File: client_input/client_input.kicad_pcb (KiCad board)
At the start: 2 copper layers, 10 parts, among them P1 CONN_01X06, P2 CONN_01X08, SW1 DIPS_08, SW2 SW_PUSH, SW3 SW_PUSH, U1 ESP-12_Breakout, U2 MCP23017, U3 MCP3208, U4 WS2812B

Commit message: PCD laid out.
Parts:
- removed U4: WS2812B, LEDs:LED_RGB_PLLC-6
- added D1: WS2812B, LEDs:LED_RGB_PLLC-6, F.Cu at (148.6, 71.1)
- added D2: Green, LEDs:LED-3MM, F.Cu at (254.6, 130.2)
- added D3: Yellow, LEDs:LED-3MM, F.Cu at (254.6, 122.6)
- added D4: Status RGB, LEDs:LED-RGB-5MM_Common_Cathode, F.Cu at (273.1, 148.6)
- added D5: Red, LEDs:LED-3MM, F.Cu at (254.6, 114.9)
- added P3: Ribbon, Socket_Strips:Socket_Strip_Straight_1x09, F.Cu at (185.4, 80.0)
- added P4: Ribbon, Socket_Strips:Socket_Strip_Straight_1x08, F.Cu at (167.6, 82.5)
- added P6: Ribbon, Socket_Strips:Socket_Strip_Straight_1x04, F.Cu at (243.8, 148.6)
- added P7: Ribbon, Socket_Strips:Socket_Strip_Straight_1x09, F.Cu at (243.8, 83.8)
- added P8: Ribbon, Socket_Strips:Socket_Strip_Straight_1x03, F.Cu at (244.5, 120.0)
- added R2: 22k, Resistors_ThroughHole:Resistor_Horizontal_RM10mm, F.Cu at (143.5, 109.2)
- added R3: 560, Resistors_ThroughHole:Resistor_Horizontal_RM10mm, F.Cu at (158.8, 109.2)
- added R4: 470, Resistors_ThroughHole:Resistor_Horizontal_RM10mm, F.Cu at (262.9, 151.1)
- added R5: 100, Resistors_ThroughHole:Resistor_Horizontal_RM10mm, F.Cu at (262.9, 141.0)
- added R6: 100, Resistors_ThroughHole:Resistor_Horizontal_RM10mm, F.Cu at (262.9, 146.1)
- added R7: 100, Resistors_ThroughHole:Resistor_Horizontal_RM10mm, F.Cu at (263.5, 130.2)
- added R8: 100, Resistors_ThroughHole:Resistor_Horizontal_RM10mm, F.Cu at (263.5, 122.6)
- added R9: 470, Resistors_ThroughHole:Resistor_Horizontal_RM10mm, F.Cu at (263.5, 114.9)
- added SW4: DIPS_08, Buttons_Switches_ThroughHole:SW_DIP_x8_Slide, F.Cu at (250.2, 83.8)
- P1: value CONN_01X06 -> Analog In; footprint Pin_Headers:Pin_Header_Angled_1x06 -> Socket_Strips:Socket_Strip_Straight_1x08
- P2: value CONN_01X08 -> FTDI; footprint Socket_Strips:Socket_Strip_Straight_1x08 -> Pin_Headers:Pin_Header_Straight_1x06
- R1: value 570 -> 100k
- SW1: value DIPS_08 -> PAIR_MODE; footprint Buttons_Switches_ThroughHole:SW_DIP_x8_Slide -> Buttons_Switches_ThroughHole:SW_TH_Tactile_Omron_B3F-10xx
- SW2: value SW_PUSH -> RESET
- SW3: value SW_PUSH -> Bootload
- U1: value ESP-12_Breakout -> MCP3208; footprint ESP8266:ESP12_Breakout -> Housings_DIP:DIP-16_W7.62mm_LongPads
- U2: value MCP23017 -> ESP-12_Breakout; footprint Housings_DIP:DIP-28_W7.62mm_LongPads -> ESP8266:ESP12_Breakout
- U3: value MCP3208 -> MCP23017; footprint Housings_DIP:DIP-18_W7.62mm_LongPads -> Housings_DIP:DIP-28_W7.62mm_LongPads
- moved U3 87.8 mm to (172.7, 80.0)
- moved SW3 50.7 mm to (147.3, 83.8), turned to 90 degrees
- moved SW2 49.9 mm to (138.4, 77.5), turned to 270 degrees
- moved U2 46.6 mm to (148.5, 105.0), turned to 270 degrees
- moved P2 37.0 mm to (116.8, 78.7), turned to 90 degrees
- moved P1 32.1 mm to (116.8, 95.2), turned to 270 degrees
- moved SW1 23.3 mm to (162.6, 77.5)
- moved R1 19.9 mm to (138.4, 109.2)
- moved U1 13.5 mm to (121.9, 95.2), turned to 0 degrees
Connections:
- P1 pad 1: GND -> Net-(P1-Pad1)
- P1 pad 3: +BATT -> Net-(P1-Pad3)
- P2 pad 1: Net-(P2-Pad1) -> GND
- P2 pad 3: Net-(P2-Pad3) -> +BATT
- R1 pad 1: Net-(R1-Pad1) -> +BATT
- R1 pad 2: Net-(R1-Pad2) -> BattSense
- SW1 pad 1: Net-(SW1-Pad1) -> Pair_sw
- SW1 pad 2: Net-(SW1-Pad2) -> GND
- SW1 pad 3: Net-(SW1-Pad3) -> (no net)
- SW1 pad 4: Net-(SW1-Pad4) -> (no net)
- U1 pad 1: Net-(SW2-Pad2) -> Net-(P1-Pad1)
- U1 pad 11: Net-(R1-Pad1) -> Net-(U1-Pad11)
- U1 pad 12: Net-(SW3-Pad1) -> Net-(U1-Pad12)
- U1 pad 14: Net-(U1-Pad14) -> GND
- U1 pad 15: Net-(P1-Pad4) -> +3V3
- U1 pad 16: Net-(P1-Pad5) -> +3V3
- U1 pad 2: BattSense -> Net-(P1-Pad2)
- U1 pad 3: Net-(U1-Pad3) -> Net-(P1-Pad3)
- U1 pad 4: Net-(U1-Pad4) -> Net-(P1-Pad4)
- U1 pad 5: Net-(U1-Pad5) -> Net-(P1-Pad5)
- U1 pad 6: Net-(U1-Pad6) -> Net-(P1-Pad6)
- U1 pad 7: Net-(U1-Pad7) -> Net-(P1-Pad7)
- U1 pad 8: +BATT -> Net-(P1-Pad8)
- U2 pad 1: Net-(U2-Pad1) -> Net-(SW2-Pad2)
- U2 pad 10: GND -> Net-(U1-Pad10)
- U2 pad 11: (no net) -> Net-(R3-Pad1)
- U2 pad 12: Net-(U1-Pad14) -> Net-(SW3-Pad1)
- U2 pad 13: Net-(U1-Pad13) -> Net-(U2-Pad13)
- U2 pad 14: (no net) -> Net-(U2-Pad14)
- U2 pad 15: GND -> Net-(P2-Pad4)
- U2 pad 16: GND -> Net-(P2-Pad5)
- U2 pad 2: Net-(U2-Pad2) -> BattSense
- U2 pad 4: Net-(U2-Pad4) -> Net-(SW2-Pad2)
- U2 pad 5: Net-(U2-Pad5) -> Net-(U1-Pad13)
- U2 pad 6: Net-(U2-Pad6) -> Net-(U1-Pad12)
- U2 pad 7: Net-(U2-Pad7) -> Net-(U1-Pad11)
- U2 pad 8: Net-(U2-Pad8) -> +BATT
- U2 pad 9: +3V3 -> GND
- U3 pad 1: Net-(P2-Pad1) -> Pair_sw
- U3 pad 10: Net-(U1-Pad10) -> GND
- U3 pad 11: Net-(U1-Pad7) -> (no net)
- U3 pad 12: Net-(U1-Pad6) -> Net-(U2-Pad14)
- U3 pad 13: Net-(U1-Pad5) -> Net-(U2-Pad13)
- U3 pad 14: GND -> (no net)
- U3 pad 15: +3V3 -> GND
- U3 pad 16: +3V3 -> GND
- U3 pad 17: (no net) -> GND
- U3 pad 18: (no net) -> +3V3
- U3 pad 2: Net-(P2-Pad2) -> Net-(P4-Pad1)
- U3 pad 3: Net-(P2-Pad3) -> Net-(P4-Pad2)
- U3 pad 4: Net-(P2-Pad4) -> Net-(P4-Pad3)
- U3 pad 5: Net-(P2-Pad5) -> Net-(P4-Pad4)
- U3 pad 6: Net-(P2-Pad6) -> Net-(P4-Pad5)
- U3 pad 7: Net-(P2-Pad7) -> Net-(P4-Pad6)
- U3 pad 8: Net-(P2-Pad8) -> Net-(P4-Pad7)
- U3 pad 9: GND -> +3V3

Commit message: Made some tweaks, outputted test gerber files (still PTH version).
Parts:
- added P9: LiPo, Socket_Strips:Socket_Strip_Straight_1x02, F.Cu at (129.5, 81.3)
- D1: footprint LEDs:LED_RGB_PLLC-6 -> LEDs:LED_NEOPIXEL
- SW1, SW2, SW3: footprint Buttons_Switches_ThroughHole:SW_TH_Tactile_Omron_B3F-10xx -> Buttons_Switches_ThroughHole:SW_PUSH_SMALL
- moved SW1 44.6 mm to (158.8, 121.9), turned to 180 degrees
- moved SW2 44.5 mm to (138.4, 121.9), turned to 180 degrees
- moved SW3 38.1 mm to (148.6, 121.9), turned to 180 degrees
- moved D1 30.1 mm to (125.6, 90.5), turned to 270 degrees
- moved P2 25.5 mm to (142.2, 81.3)
- moved P4 4.58 mm to (170.2, 86.4)
- moved P3 4.58 mm to (188.0, 83.8)
- moved U3 4.58 mm to (175.3, 83.8)
- moved P1 3.81 mm to (116.8, 99.1)
- moved R3 3.81 mm to (154.9, 109.2)
- moved U1 3.81 mm to (121.9, 99.1)
- moved R2 1.27 mm to (144.8, 109.2)
- moved R1 1.27 mm to (139.7, 109.2)
- moved U2 0.43 mm to (148.6, 105.4)
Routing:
- net GND: track 0.00 -> 157.2 mm
- net Pair_sw: track 0.00 -> 88.9 mm
- net +3V3: track 0.00 -> 78.7 mm
- net Net-(U1-Pad10): track 0.00 -> 61.0 mm
- net Net-(SW2-Pad2): track 0.00 -> 55.7 mm
- net +BATT: track 0.00 -> 38.3 mm
- net Net-(D1-Pad4): track 0.00 -> 36.1 mm
- net Net-(SW3-Pad1): track 0.00 -> 33.0 mm
- net Net-(P2-Pad4): track 0.00 -> 30.5 mm
- net Net-(P2-Pad5): track 0.00 -> 25.4 mm
- net Net-(U2-Pad14): track 0.00 -> 22.9 mm
- net Net-(U2-Pad13): track 0.00 -> 22.9 mm
- net BattSense: track 0.00 -> 10.1 mm
- net Net-(R3-Pad1): track 0.00 -> 7.62 mm
- net Net-(U1-Pad13): track 0.00 -> 5.18 mm
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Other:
- board outline added: 81.3 x 52.1 mm
- net class Default: trace_width 0.25 -> 1

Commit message: version 2.0, lots of changes. (smd parts, 2 sided, production ready)
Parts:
- removed D2: Green, LEDs:LED-3MM
- removed D3: Yellow, LEDs:LED-3MM
- removed D4: Status RGB, LEDs:LED-RGB-5MM_Common_Cathode
- removed D5: Red, LEDs:LED-3MM
- removed P3: Ribbon, Socket_Strips:Socket_Strip_Straight_1x09
- removed R5, R6, R7, R8: 100, Resistors_ThroughHole:Resistor_Horizontal_RM10mm
- removed R9: 470, Resistors_ThroughHole:Resistor_Horizontal_RM10mm
- removed SW4: DIPS_08, Buttons_Switches_ThroughHole:SW_DIP_x8_Slide
- added ?: BATT/FTDI, Buttons_Switches_ThroughHole:SW_Micro_SPST, F.Cu at (13.1, 4.38)
- added C1: 2.2uF, Capacitors_ThroughHole:C_Disc_D3_P2.5, F.Cu at (13.1, 19.6)
- added P5: LiPo, Socket_Strips:Socket_Strip_Straight_1x02, F.Cu at (6.76, 4.38)
- added RR1: 10k, Resistors_ThroughHole:Resistor_Array_SIP5, F.Cu at (23.2, 19.6)
- added SW5: , Buttons_Switches_ThroughHole:SW_Micro_SPST, F.Cu at (13.1, 1.84)
- added U4: MCP1700-3302, TO_SOT_Packages_SMD:SOT89-3_Housing_Handsoldering, B.Cu at (7.25, 18.4)
- added U5: MCP23017, Housings_SOIC:SOIC-28_7.5x17.9mm_Pitch1.27mm, F.Cu at (36.6, 17.7)
- added U6: MCP23017, Housings_SOIC:SOIC-28_7.5x17.9mm_Pitch1.27mm, F.Cu at (36.6, 38.0)
- P1: value Analog In -> Analog In 7-0
- P2: value FTDI -> Analog In 15-8; footprint Pin_Headers:Pin_Header_Straight_1x06 -> Socket_Strips:Socket_Strip_Straight_1x08
- P4: value Ribbon -> FTDI; footprint Socket_Strips:Socket_Strip_Straight_1x08 -> Pin_Headers:Pin_Header_Straight_1x06
- P6: value Ribbon -> i/o 0-7; footprint Socket_Strips:Socket_Strip_Straight_1x04 -> Socket_Strips:Socket_Strip_Straight_1x09
- P7: value Ribbon -> i/o 9-15; footprint Socket_Strips:Socket_Strip_Straight_1x09 -> Socket_Strips:Socket_Strip_Straight_1x08
- P8: value Ribbon -> i/o 15-23; footprint Socket_Strips:Socket_Strip_Straight_1x03 -> Socket_Strips:Socket_Strip_Straight_1x09
- P9: value LiPo -> i/o 24-31; footprint Socket_Strips:Socket_Strip_Straight_1x02 -> Socket_Strips:Socket_Strip_Straight_1x09
- R1: value 100k -> 10k; footprint Resistors_ThroughHole:Resistor_Horizontal_RM10mm -> Discret:R4
- R2: value 22k -> 560; footprint Resistors_ThroughHole:Resistor_Horizontal_RM10mm -> Discret:R4
- R3: value 560 -> 100k; footprint Resistors_ThroughHole:Resistor_Horizontal_RM10mm -> Discret:R4
- R4: value 470 -> 22k; footprint Resistors_ThroughHole:Resistor_Horizontal_RM10mm -> Discret:R4
- SW1: value PAIR_MODE -> RST
- SW2: value RESET -> PAIR
- SW3: value Bootload -> BTLD
- U1: footprint Housings_DIP:DIP-16_W7.62mm_LongPads -> Housings_SOIC:SOIC-16_3.9x9.9mm_Pitch1.27mm
- U2: value ESP-12_Breakout -> MCP3208; footprint ESP8266:ESP12_Breakout -> Housings_SOIC:SOIC-16_3.9x9.9mm_Pitch1.27mm
- U3: value MCP23017 -> ESP-12E; footprint Housings_DIP:DIP-28_W7.62mm_LongPads -> ESP8266:ESP-12E_Brendan; moved to B.Cu
- moved R4 286.9 mm to (10.6, 14.5), turned to 0 degrees
- moved P6 260.8 mm to (23.2, 9.46), turned to 0 degrees
- moved P8 238.9 mm to (23.2, 29.8), turned to 0 degrees
- moved P7 225.6 mm to (25.8, 26.0), turned to 0 degrees
- moved SW1 179.3 mm to (24.0, 3.66), turned to 0 degrees
- moved U3 175.8 mm to (5.21, 39.1)
- moved R3 174.1 mm to (10.6, 12.0), turned to 0 degrees
- moved P4 170.8 mm to (18.2, 8.57)
- moved SW3 165.5 mm to (32.9, 3.66), turned to 0 degrees
- moved U2 158.3 mm to (7.90, 33.0), turned to 0 degrees
- moved SW2 152.7 mm to (41.8, 3.66), turned to 0 degrees
- moved P2 150.3 mm to (1.55, 28.5), turned to 270 degrees
- moved P1 146.8 mm to (1.55, 8.19)
- moved R1 145.7 mm to (25.8, 18.4)
- moved R2 141.2 mm to (23.2, 37.4), turned to 270 degrees
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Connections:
- D1 pad 1: +BATT -> +Vin
- P2 pad 1: GND -> Net-(P2-Pad1)
- P2 pad 3: +BATT -> Net-(P2-Pad3)
- P4 pad 1: Net-(P4-Pad1) -> GND
- P4 pad 3: Net-(P4-Pad3) -> FTDI_VCC
- P6 pad 4: +3V3 -> Net-(P6-Pad4)
- P7 pad 8: Net-(P7-Pad8) -> +3V3
- P9 pad 1: GND -> Net-(P9-Pad1)
- P9 pad 2: +BATT -> Net-(P9-Pad2)
- R1 pad 1: +BATT -> SPI_SS
- R1 pad 2: BattSense -> GND
- R2 pad 1: GND -> LED_stat
- R2 pad 2: BattSense -> Net-(D1-Pad4)
- R3 pad 1: Net-(R3-Pad1) -> +BATT
- R3 pad 2: Net-(D1-Pad4) -> BattSense
- R4 pad 1: Net-(D4-Pad1) -> GND
- R4 pad 2: Net-(P6-Pad1) -> BattSense
- SW1 pad 1: Pair_sw -> RST
- SW2 pad 1: GND -> Pair_sw
- SW2 pad 2: Net-(SW2-Pad2) -> GND
- SW3 pad 1: Net-(SW3-Pad1) -> BL_sw
- U1 pad 10: Net-(U1-Pad10) -> SPI_SS
- U1 pad 11: Net-(U1-Pad11) -> MOSI
- U1 pad 12: Net-(U1-Pad12) -> MISO
- U1 pad 13: Net-(U1-Pad13) -> SPI_CLK
- U2 pad 1: Net-(SW2-Pad2) -> Net-(P2-Pad1)
- U2 pad 10: Net-(U1-Pad10) -> Net-(P7-Pad1)
- U2 pad 11: Net-(R3-Pad1) -> MOSI
- U2 pad 12: Net-(SW3-Pad1) -> MISO
- U2 pad 13: Net-(U2-Pad13) -> SPI_CLK
- U2 pad 14: Net-(U2-Pad14) -> GND
- U2 pad 15: Net-(P2-Pad4) -> +3V3
- U2 pad 16: Net-(P2-Pad5) -> +3V3
- U2 pad 2: BattSense -> Net-(P2-Pad2)
- U2 pad 3: Net-(U2-Pad3) -> Net-(P2-Pad3)
- U2 pad 4: Net-(SW2-Pad2) -> Net-(P2-Pad4)
- U2 pad 5: Net-(U1-Pad13) -> Net-(P2-Pad5)
- U2 pad 6: Net-(U1-Pad12) -> Net-(P2-Pad6)
- U2 pad 7: Net-(U1-Pad11) -> Net-(P2-Pad7)
- U2 pad 8: +BATT -> Net-(P2-Pad8)
- U3 pad 1: Pair_sw -> RST
- U3 pad 10: GND -> SPI_SS
- U3 pad 11: (no net) -> LED_stat
- U3 pad 12: Net-(U2-Pad14) -> BL_sw
- U3 pad 13: Net-(U2-Pad13) -> SDA
- U3 pad 14: (no net) -> SCL
- U3 pad 15: GND -> Net-(P4-Pad4)
- U3 pad 16: GND -> Net-(P4-Pad5)
- U3 pad 2: Net-(P4-Pad1) -> BattSense
- U3 pad 3: Net-(P4-Pad2) -> CH_PD
- U3 pad 4: Net-(P4-Pad3) -> RST
- U3 pad 5: Net-(P4-Pad4) -> SPI_CLK
- U3 pad 6: Net-(P4-Pad5) -> MISO
- U3 pad 7: Net-(P4-Pad6) -> MOSI
- U3 pad 8: Net-(P4-Pad7) -> +3V3
- U3 pad 9: +3V3 -> GND
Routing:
- net GND: track 157.2 -> 56.7 mm, vias 0 -> 6
- net RST: track 0.00 -> 64.8 mm
- net Pair_sw: track 88.9 -> 25.3 mm
- net Net-(U1-Pad10): track 61.0 -> 0.00 mm
- net Net-(SW2-Pad2): track 55.7 -> 0.00 mm
- net SDA: track 0.00 -> 55.2 mm, vias 0 -> 1
- net SCL: track 0.00 -> 50.6 mm, vias 0 -> 1
- net +Vin: track 0.00 -> 44.0 mm, vias 0 -> 2
- net BL_sw: track 0.00 -> 39.0 mm, vias 0 -> 1
- net +3V3: track 78.7 -> 115.4 mm, vias 0 -> 3
- net CH_PD: track 0.00 -> 33.1 mm
- net Net-(SW3-Pad1): track 33.0 -> 0.00 mm
- net Net-(P4-Pad5): track 5.08 -> 35.3 mm, vias 0 -> 1
- net Net-(P7-Pad1): track 0.00 -> 27.9 mm
- net BattSense: track 10.1 -> 37.4 mm, vias 0 -> 1
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- added copper zone on B.Cu, net GND
- added copper zone on F.Cu, net GND
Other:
- board size 81.3 x 52.1 mm -> 46.5 x 47.8 mm
- net class Default: clearance 0.2 -> 0.1524; trace_width 1 -> 0.1524; via_dia 0.6 -> 0.6858; via_drill 0.4 -> 0.3302
- rule trace_clearance: 0.2 -> 0.1524
- rule trace_min: 0.2 -> 0.1524
- rule via_min_drill: 0.3 -> 0.3302
- rule via_min_size: 0.4 -> 0.6858
- board text added: "TCT v2.0 3.3-6.0v, 250mA c. 2016 Tangible Interaction"

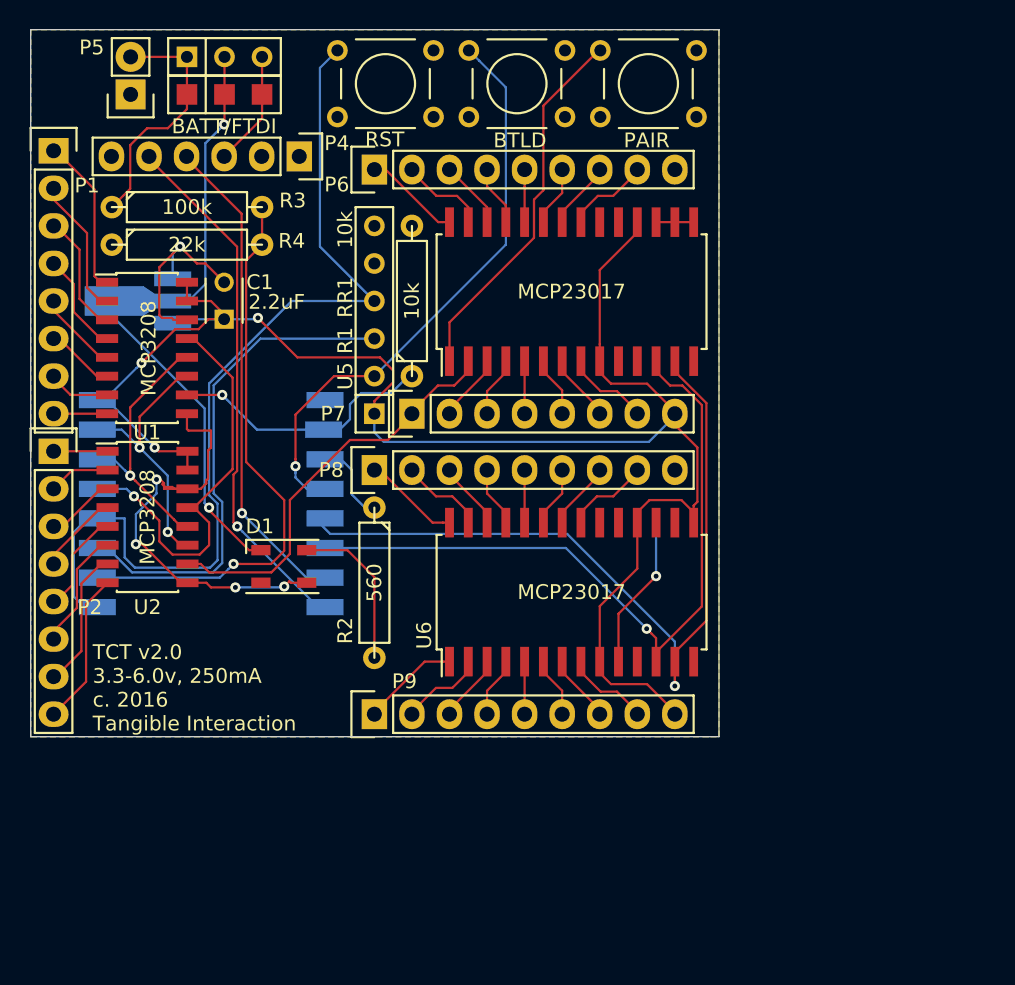
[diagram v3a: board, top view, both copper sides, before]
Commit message: totally screwed up stitching vias and then fixed them
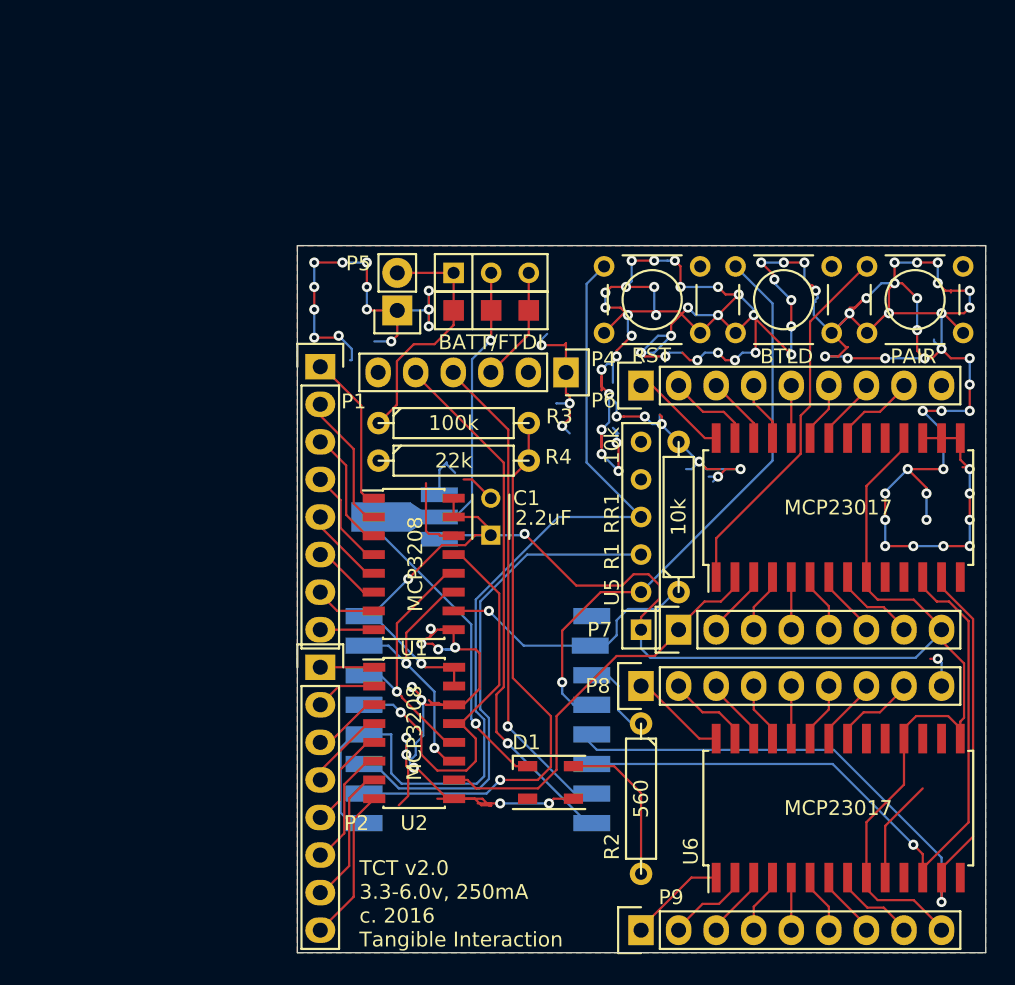
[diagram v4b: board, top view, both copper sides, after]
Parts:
- moved C1 23.2 mm to (31.1, 34.2)
- moved D1 23.2 mm to (35.2, 50.9)
- moved P1 23.2 mm to (19.6, 22.8)
- moved P2 23.2 mm to (19.6, 43.1)
- moved P5 23.2 mm to (24.8, 19.0)
- moved P7 23.2 mm to (43.8, 40.6)
- moved P9 23.2 mm to (41.3, 60.9)
- moved R2 23.2 mm to (41.3, 52.0)
- moved SW1 23.2 mm to (42.0, 18.3)
- moved U1 23.2 mm to (25.9, 36.1)
- moved U2 23.2 mm to (25.9, 47.6)
- moved U6 23.2 mm to (54.6, 52.6)
- moved ? 23.2 mm to (31.1, 19.0)
- moved P4 23.2 mm to (36.2, 23.2)
- moved P6 23.2 mm to (41.3, 24.1)
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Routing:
- net GND: track 56.7 -> 319.0 mm, vias 6 -> 108
- net +3V3: track 115.4 -> 116.1 mm

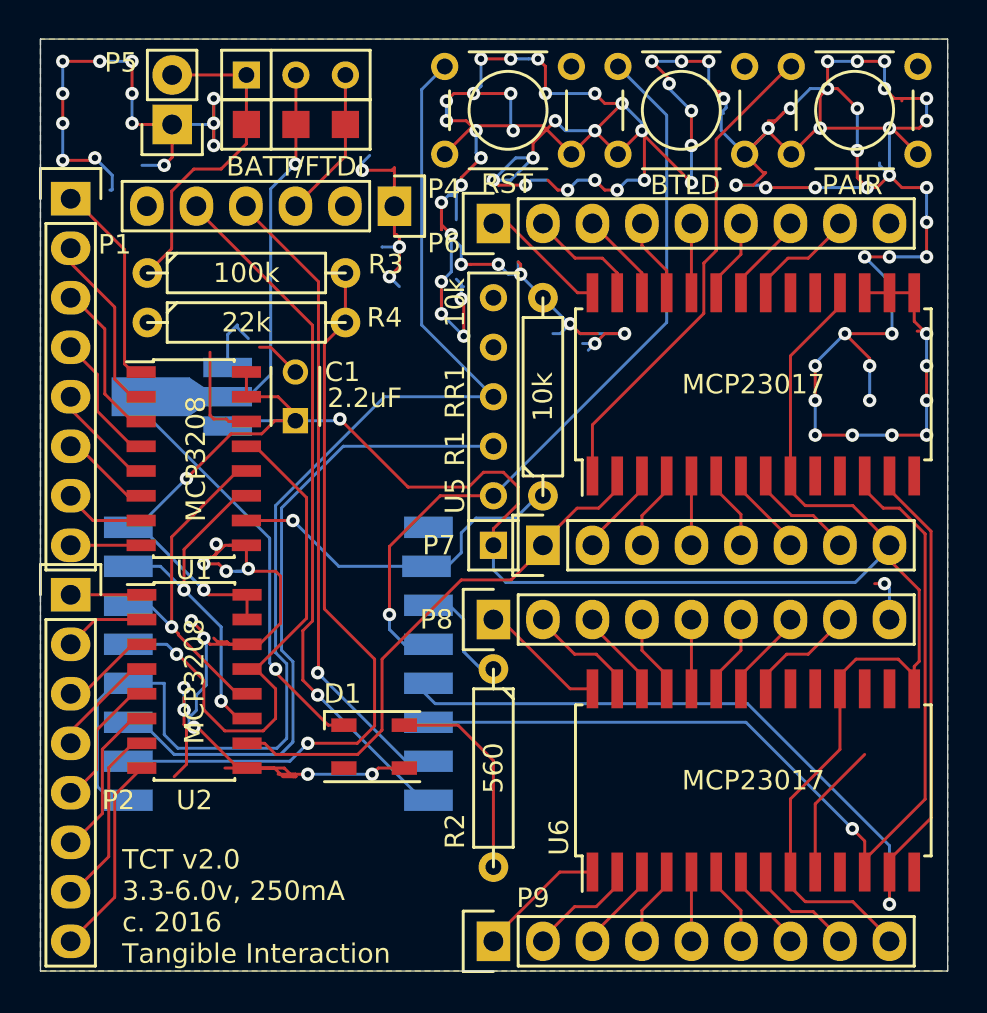
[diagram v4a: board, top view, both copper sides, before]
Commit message: finished re-doing stitching vias
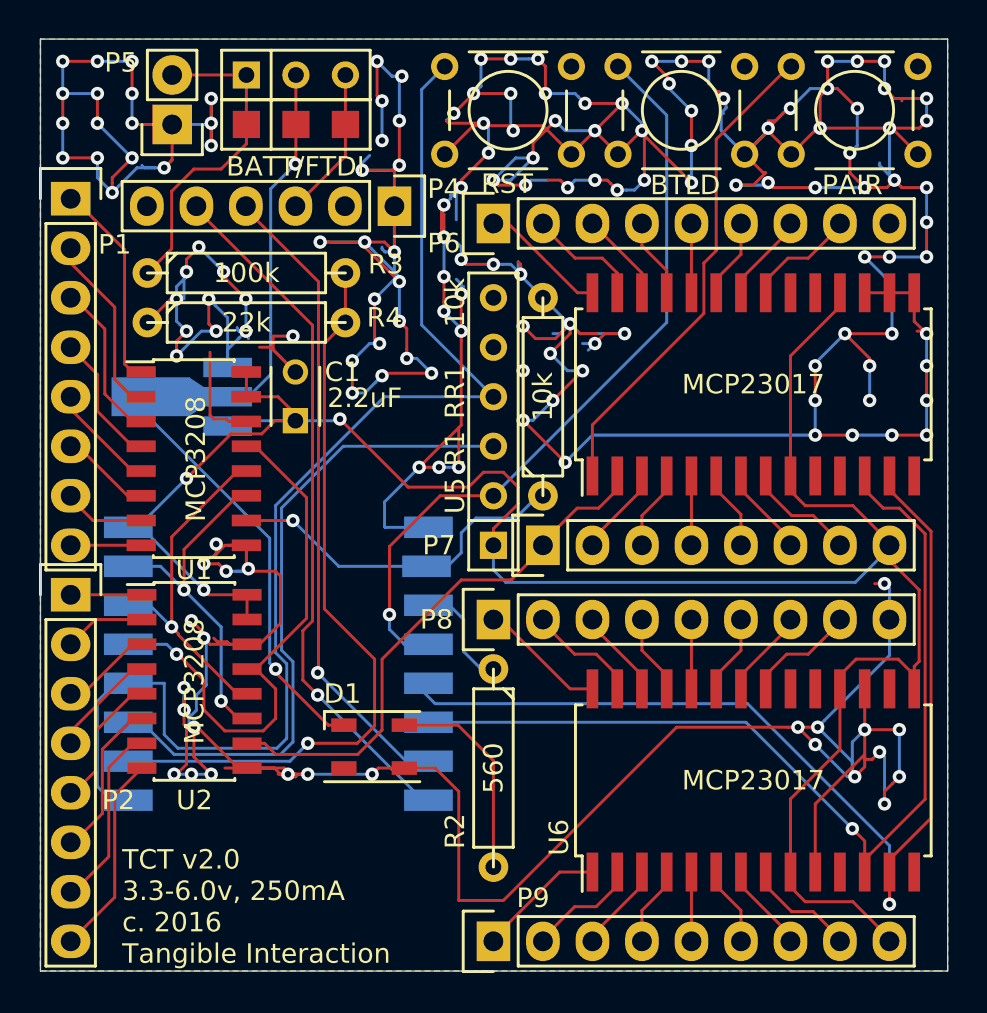
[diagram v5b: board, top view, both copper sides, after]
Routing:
- net GND: track 319.0 -> 516.2 mm, vias 108 -> 161
